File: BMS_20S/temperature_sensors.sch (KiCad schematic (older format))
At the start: 27 parts, among them J2101 TEMP_IDC_26_CONN

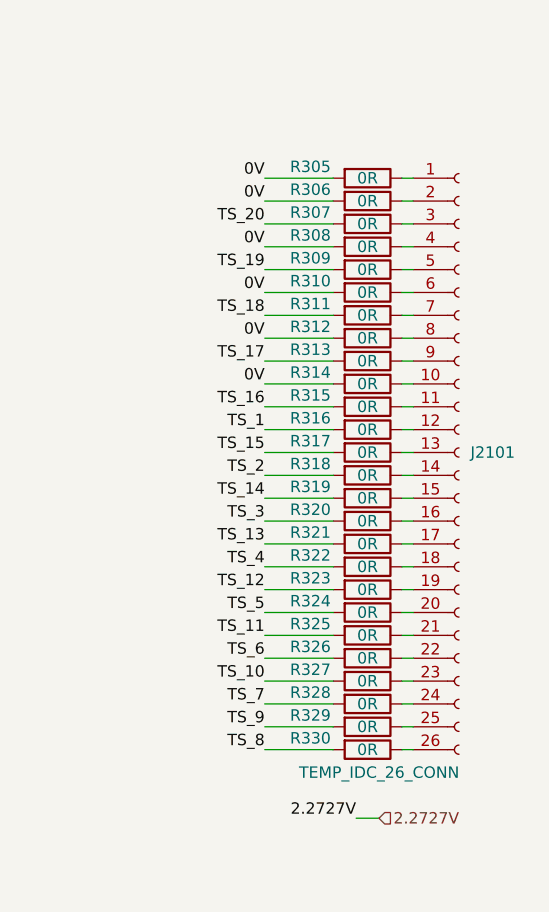
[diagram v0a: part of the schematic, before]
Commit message: add current sense block to the schematic
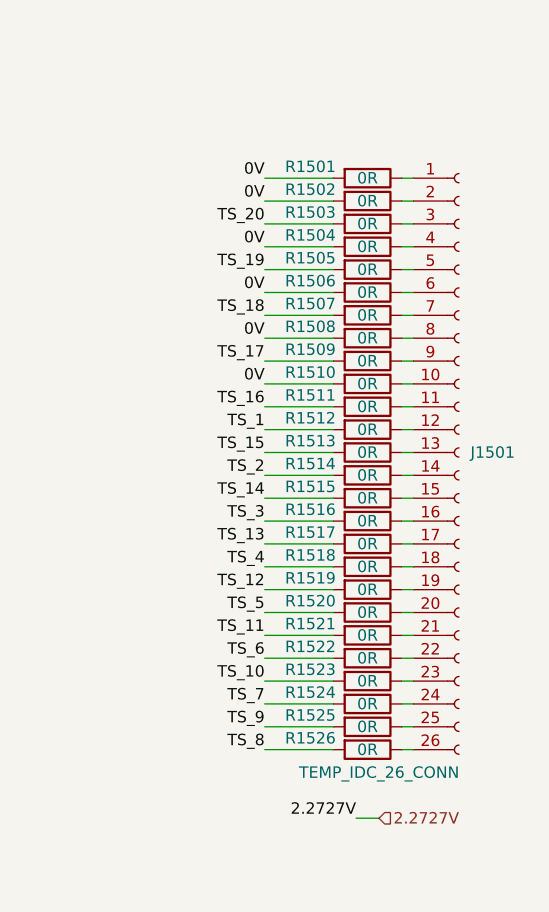
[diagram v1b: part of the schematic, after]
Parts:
- renumbered J2101 to J1501, R305 to R1501, R306 to R1502, R307 to R1503, R308 to R1504, R309 to R1505, R310 to R1506, R311 to R1507, R312 to R1508, R313 to R1509, R314 to R1510, R315 to R1511, R316 to R1512, R317 to R1513, R318 to R1514, R319 to R1515, R320 to R1516, R321 to R1517, R322 to R1518, R323 to R1519, R324 to R1520, R325 to R1521, R326 to R1522, R327 to R1523, R328 to R1524, R329 to R1525, R330 to R1526
